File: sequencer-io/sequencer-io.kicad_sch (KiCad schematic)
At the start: 97 parts, among them SW1 SW_Push, SW10 SW_Push, SW11 SW_Push, SW12 SW_Push, SW13 SW_Push, SW14 SW_Push, SW15 SW_Push, SW16 SW_Push, SW17 SW_Push, SW18 SW_Push, SW19 SW_Push, SW2 SW_Push, SW20 SW_Push, SW21 SW_Push, SW22 SW_Push, SW23 SW_Push, SW24 RotaryEncoder, SW3 SW_Push, SW4 SW_Push, SW5 SW_Push, SW6 SW_Push, SW7 SW_Push, SW8 SW_Push, SW9 SW_Push, U2 74HC595, U20 SC0915

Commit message: Edited PCB
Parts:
- added D24: 1N4148W, Diode_SMD:D_SOD-323_HandSoldering, symbol Diode:1N4148W
- U20: footprint SC0915:MODULE_SC0915 -> SC0915:SC0915
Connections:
- net +5V: now also U20.40 (VBUS), D24.2 (A)
- net COL0: now also U20.21 (GP16); no longer U20.10 (GP7)
- net COL1: now also U20.22 (GP17); no longer U20.9 (GP6)
- net COL2: now also U20.24 (GP18); no longer U20.7 (GP5)
- net COL3: now also U20.25 (GP19); no longer U20.6 (GP4)
- net COL4: now also U20.26 (GP20); no longer U20.5 (GP3)
- net COL5: now also U20.27 (GP21); no longer U20.4 (GP2)
- net COL6: now also U20.29 (GP22); no longer U20.2 (GP1)
- net COL7: now also U20.31 (GP26); no longer U20.1 (GP0)
- net DIGIT_1: now also U20.17 (GP13)
- net DIGIT_2: now also U20.16 (GP12)
- net DIGIT_3: now also U20.15 (GP11)
- net ENC_A: now also U20.19 (GP14)
- net ENC_B: now also U20.20 (GP15)
- net GND: now also U20.13 (GND), U20.18 (GND), U20.23 (GND), U20.28 (GND), U20.3 (GND), U20.33 (AGND), U20.38 (GND), U20.8 (GND), U20.D2 (GND)
- net PXL: now also U20.34 (GP28); no longer U20.16 (GP12)
- net ROW0: now also U20.4 (GP2); no longer U20.11 (GP8)
- net ROW1: now also U20.5 (GP3); no longer U20.12 (GP9)
- net ROW2: now also U20.6 (GP4); no longer U20.14 (GP10)
- net ROW3: now also U20.7 (GP5); no longer U20.15 (GP11)
- net VSYS: now reaches U20.39 (VSYS)
- net VSYS: now also D24.1 (K)
- no-connect marks 1 -> 2

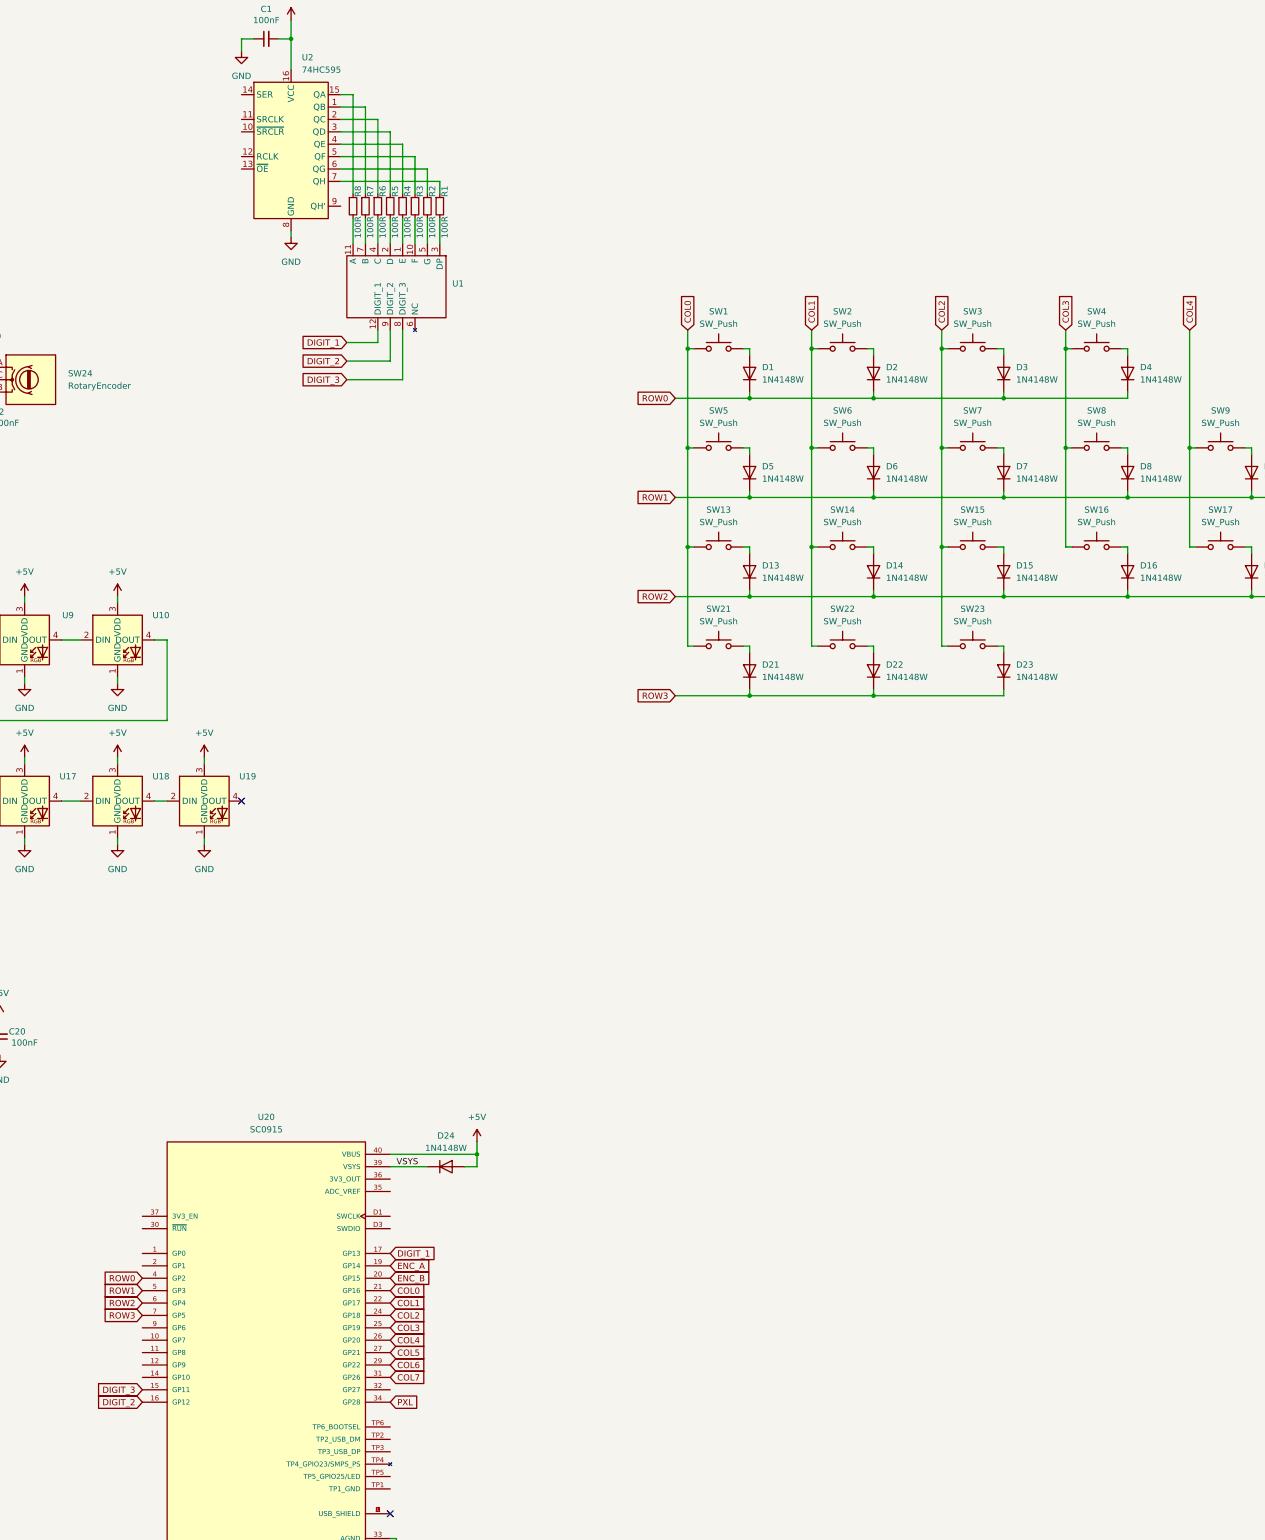
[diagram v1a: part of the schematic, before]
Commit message: Added TCA8418
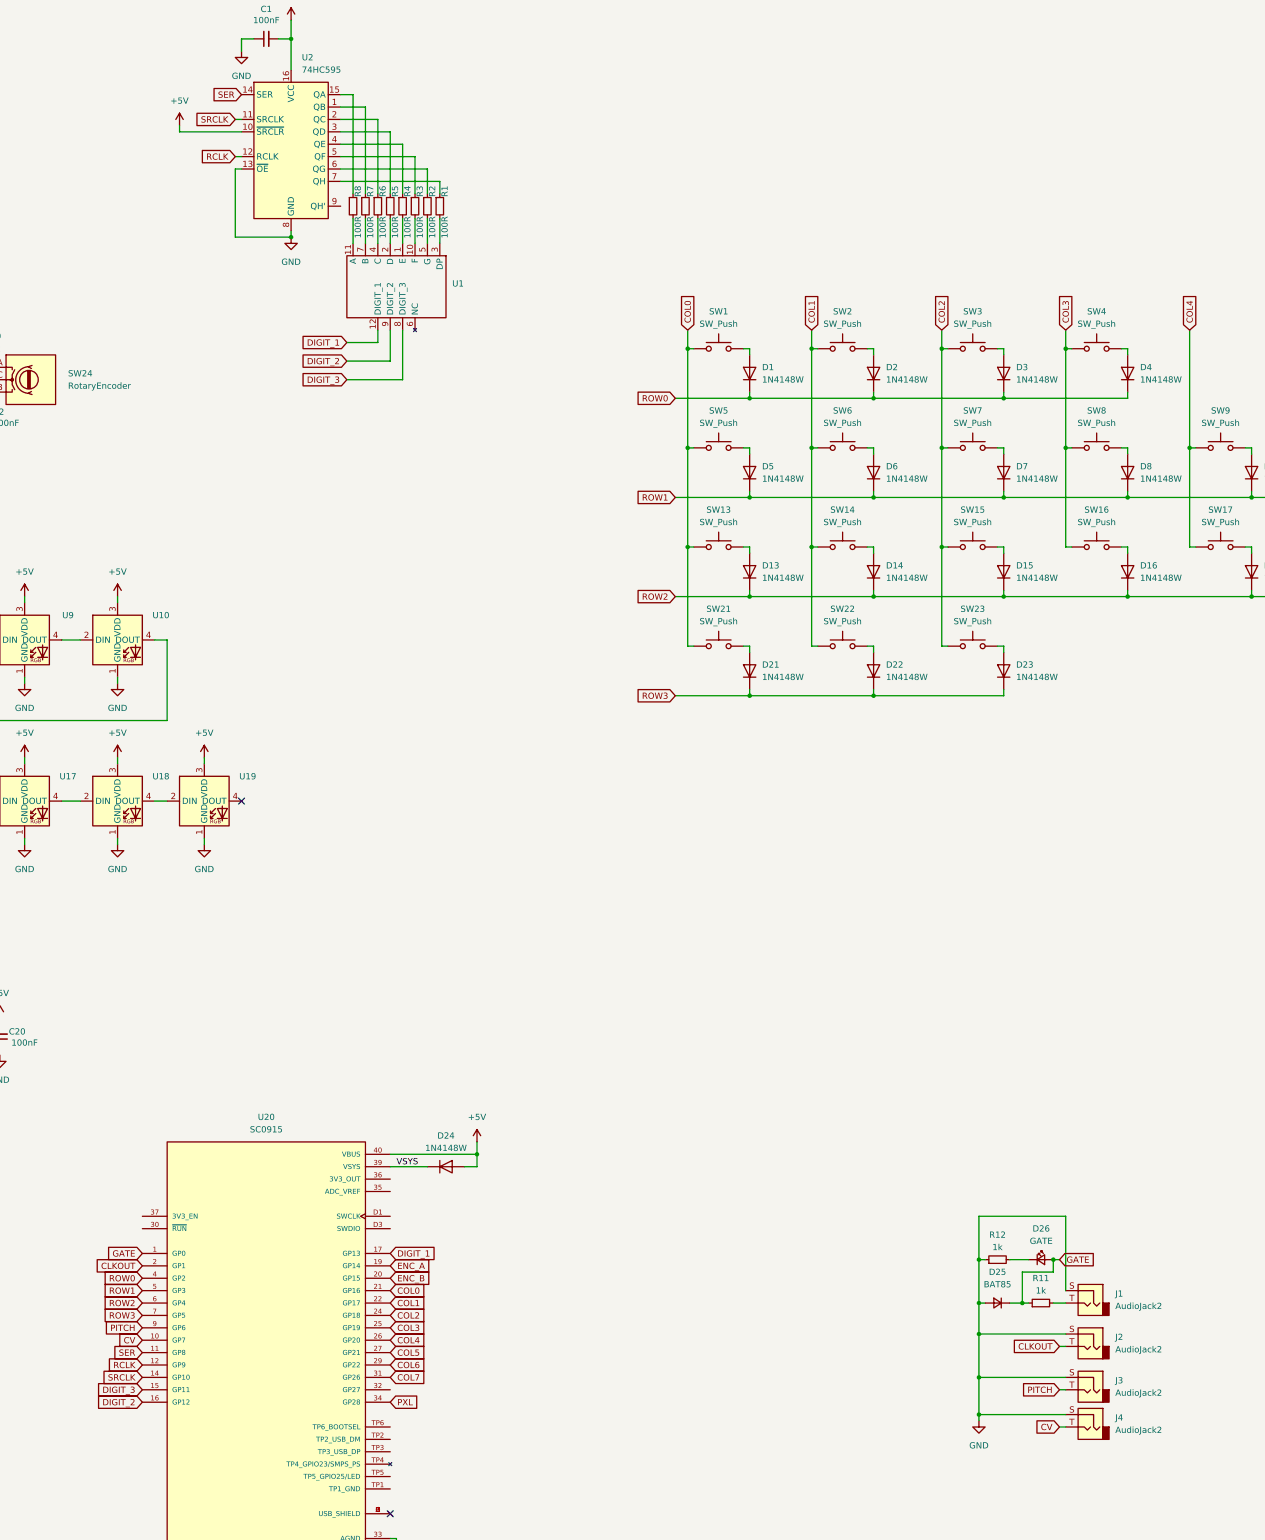
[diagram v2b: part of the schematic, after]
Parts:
- added D25: BAT85, symbol Device:D_Small
- added D26: GATE, symbol Device:LED_Small
- added J1, J2, J3, J4: AudioJack2, symbol Connector_Audio:AudioJack2
- added R11, R12: 1k, symbol Device:R_Small
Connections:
- net +5V: now also U2.10 (~{SRCLR})
- net GND: now also U2.13 (~{OE}), D25.2 (A), J1.S, J2.S, J3.S, J4.S, R12.1
- net GATE: now reaches U20.1 (GP0)
- net GATE: now also D25.1 (K), D26.2 (A), R11.1
- net CV: now reaches U20.10 (GP7)
- net CV: now also J4.T
- net SER: now reaches U20.11 (GP8)
- net SER: now also U2.14 (SER)
- net RCLK: now reaches U20.12 (GP9)
- net RCLK: now also U2.12 (RCLK)
- net SRCLK: now reaches U20.14 (GP10)
- net SRCLK: now also U2.11 (SRCLK)
- net CLKOUT: now reaches U20.2 (GP1)
- net CLKOUT: now also J2.T
- net PITCH: now reaches U20.9 (GP6)
- net PITCH: now also J3.T
- new net: J1.T, R11.2
- new net: D26.1 (K), R12.2

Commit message: Cleaned up schematic, added DAC and outputs
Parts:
- removed C1, C10, C11, C12, C13, C14, C15, C16, C17, C18, C19, C2, C20, C3, C4, C5, C6, C7, C8, C9: 100nF, Capacitor_SMD:C_0603_1608Metric_Pad1.08x0.95mm_HandSolder, symbol Device:C_Small
- removed D1, D10, D11, D12, D13, D14, D15, D16, D17, D18, D19, D2, D20, D21, D22, D23, D24, D3, D4, D5, D6, D7, D8, D9: 1N4148W, Diode_SMD:D_SOD-323_HandSoldering, symbol Diode:1N4148W
- removed D25: BAT85, symbol Device:D_Small
- removed D26: GATE, symbol Device:LED_Small
- removed J1, J2, J3, J4: AudioJack2, symbol Connector_Audio:AudioJack2
- removed R1, R2, R3, R4, R5, R6, R7, R8: 100R, Resistor_SMD:R_0603_1608Metric_Pad0.98x0.95mm_HandSolder, symbol Device:R_Small
- removed R10, R9: 1k, Resistor_SMD:R_0603_1608Metric_Pad0.98x0.95mm_HandSolder, symbol Device:R_Small
- removed R11, R12: 1k, symbol Device:R_Small
- removed SW1, SW10, SW11, SW12, SW13, SW14, SW15, SW16, SW17, SW18, SW19, SW2, SW20, SW23, SW3, SW4, SW5, SW6, SW7, SW8, SW9: SW_Push, PCM_Switch_Keyboard_Cherry_MX:SW_Cherry_MX_PCB_1.00u, symbol Switch:SW_Push
- removed SW21, SW22: SW_Push, PCM_Switch_Keyboard_Cherry_MX:SW_Cherry_MX_PCB_2.00u, symbol Switch:SW_Push
- removed SW24: RotaryEncoder, EC12E2430404:EC12E2430404, symbol Device:RotaryEncoder
- removed U1: ~, FJ5361BH:FJ5361BH, symbol FJ5361BH:FJ5361BH
- removed U10, U11, U12, U13, U14, U15, U16, U17, U18, U19, U3, U4, U5, U6, U7, U8, U9: ~, SK6812MINI-E-012:SK6812MINI-E-012, symbol SK6812MINI-E-012:SK6812MINI-E-012
- removed U2: 74HC595, Package_SO:SOIC-16_3.9x9.9mm_P1.27mm, symbol 74xx:74HC595
- added C21: 47uF, Capacitor_SMD:C_0603_1608Metric_Pad1.08x0.95mm_HandSolder, symbol Device:C_Small
- added D26: SS34F, Diode_SMD:D_SMA_Handsoldering, symbol Device:D_Schottky_Small
- added J7: 5V EXT, Connector_PinHeader_2.54mm:PinHeader_1x02_P2.54mm_Vertical, symbol Connector_Generic:Conn_01x02
- added Q7: DMG2305UX-7, Package_TO_SOT_SMD:SOT-23, symbol Device:Q_PMOS_GSD
- added R19, R20: 10k, Resistor_SMD:R_0603_1608Metric_Pad0.98x0.95mm_HandSolder, symbol Device:R_Small
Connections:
- net VSYS is gone; now on net +5V: U20.39 (VSYS)
- net +5V: now also C21.2, D26.1 (K), Q7.2 (S); no longer U20.40 (VBUS)
- net GND: now also C21.1, J7.2 (Pin_2)
- net CLKOUT: no longer names the net of U20.2 (GP1)
- net COL0: no longer names the net of U20.21 (GP16)
- net COL1: no longer names the net of U20.22 (GP17)
- net COL2: no longer names the net of U20.24 (GP18)
- net COL3: no longer names the net of U20.25 (GP19)
- net COL4: no longer names the net of U20.26 (GP20)
- net COL5: no longer names the net of U20.27 (GP21)
- net COL6: no longer names the net of U20.29 (GP22)
- net COL7: no longer names the net of U20.31 (GP26)
- net CV: no longer names the net of U20.10 (GP7)
- net DIGIT_1: no longer names the net of U20.17 (GP13)
- net DIGIT_2: no longer names the net of U20.16 (GP12)
- net DIGIT_3: no longer names the net of U20.15 (GP11)
- net ENC_A: no longer names the net of U20.19 (GP14)
- net ENC_B: no longer names the net of U20.20 (GP15)
- net GATE: no longer names the net of U20.1 (GP0)
- net PITCH: no longer names the net of U20.9 (GP6)
- net PXL: no longer names the net of U20.34 (GP28)
- net RCLK: no longer names the net of U20.12 (GP9)
- net ROW0: no longer names the net of U20.4 (GP2)
- net ROW1: no longer names the net of U20.5 (GP3)
- net ROW2: no longer names the net of U20.6 (GP4)
- net ROW3: no longer names the net of U20.7 (GP5)
- net SER: no longer names the net of U20.11 (GP8)
- net SRCLK: no longer names the net of U20.14 (GP10)
- new net: D26.2 (A), Q7.1 (G), U20.40 (VBUS)
- new net: J7.1 (Pin_1), Q7.3 (D)
- new net +3.3V: R19.1, R20.1
- new net Switches/SCL: R20.2
- new net Switches/SDA: R19.2
- no-connect marks 2 -> 7
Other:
- added sheet DAC (dac.kicad_sch)
- added sheet IOs (ios.kicad_sch)
- added sheet LEDs (leds.kicad_sch)
- added sheet Switches (switches.kicad_sch)
- moved on the sheet: U20

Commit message: lil update
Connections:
- net LEDs/PXL: now also U20.20 (GP15)
- net Switches/SCL: now also U20.2 (GP1)
- net Switches/SDA: now also U20.1 (GP0)
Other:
- moved on the sheet: C21, D26, J7, Q7, U20

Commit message: edits
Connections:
- net IOs/DIGIT_1: now also U20.26 (GP20)
- net IOs/DIGIT_2: now also U20.25 (GP19)
- net IOs/DIGIT_3: now also U20.24 (GP18)
- net IOs/ENC_A: now also U20.20 (GP15)
- net IOs/ENC_B: now also U20.19 (GP14)
- net LEDs/PXL: now also U20.34 (GP28); no longer U20.20 (GP15)
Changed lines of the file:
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@@
+	(wire
+		(pts
+			(xy 85.09 80.01) (xy 85.09 137.16)
+		)
+		(stroke
+			(width 0)
+			(type default)
+		)
+	)
 	(wire
 		(pts
@@
 	(wire
 		(pts
+			(xy 63.5 95.25) (xy 82.55 95.25)
+		)
+		(stroke
+			(width 0)
+			(type default)
+		)
+	)
+	(wire
+		(pts
 			(xy 161.29 36.83) (xy 161.29 38.1)
 		)
@@
 	(wire
 		(pts
+			(xy 87.63 134.62) (xy 151.13 134.62)
+		)
+		(stroke
+			(width 0)
+			(type default)
+		)
+	)
+	(wire
+		(pts
 			(xy 69.85 123.19) (xy 63.5 123.19)
 		)
@@
 	(wire
 		(pts
+			(xy 153.67 77.47) (xy 153.67 137.16)
+		)
+		(stroke
+			(width 0)
+			(type default)
+		)
+	)
+	(wire
+		(pts
 			(xy 67.31 142.24) (xy 67.31 85.09)
 		)
@@
 	(wire
 		(pts
+			(xy 83.82 92.71) (xy 83.82 138.43)
+		)
+		(stroke
+			(width 0)
+			(type default)
+		)
+	)
+	(wire
+		(pts
+			(xy 152.4 135.89) (xy 152.4 80.01)
+		)
+		(stroke
+			(width 0)
+			(type default)
+		)
+	)
+	(wire
+		(pts
 			(xy 175.26 34.29) (xy 181.61 34.29)
 		)
@@
 	(wire
 		(pts
+			(xy 82.55 139.7) (xy 156.21 139.7)
+		)
+		(stroke
+			(width 0)
+			(type default)
+		)
+	)
+	(wire
+		(pts
 			(xy 144.78 125.73) (xy 146.05 125.73)
 		)
@@
 	(wire
 		(pts
+			(xy 85.09 137.16) (xy 153.67 137.16)
+		)
+		(stroke
+			(width 0)
+			(type default)
+		)
+	)
+	(wire
+		(pts
+			(xy 86.36 135.89) (xy 152.4 135.89)
+		)
+		(stroke
+			(width 0)
+			(type default)
+		)
+	)
+	(wire
+		(pts
+			(xy 151.13 82.55) (xy 151.13 134.62)
+		)
+		(stroke
+			(width 0)
+			(type default)
+		)
+	)
+	(wire
+		(pts
+			(xy 63.5 74.93) (xy 87.63 74.93)
+		)
+		(stroke
+			(width 0)
+			(type default)
+		)
+	)
+	(wire
+		(pts
 			(xy 73.66 52.07) (xy 73.66 53.34)
 		)
@@
 	(wire
 		(pts
+			(xy 152.4 80.01) (xy 144.78 80.01)
+		)
+		(stroke
+			(width 0)
+			(type default)
+		)
+	)
+	(wire
+		(pts
 			(xy 64.77 64.77) (xy 93.98 64.77)
 		)
@@
 	(wire
 		(pts
+			(xy 156.21 139.7) (xy 156.21 67.31)
+		)
+		(stroke
+			(width 0)
+			(type default)
+		)
+	)
+	(wire
+		(pts
 			(xy 64.77 58.42) (xy 64.77 64.77)
 		)
@@
 	(wire
 		(pts
+			(xy 63.5 92.71) (xy 83.82 92.71)
+		)
+		(stroke
+			(width 0)
+			(type default)
+		)
+	)
+	(wire
+		(pts
+			(xy 86.36 77.47) (xy 86.36 135.89)
+		)
+		(stroke
+			(width 0)
+			(type default)
+		)
+	)
+	(wire
+		(pts
 			(xy 160.02 36.83) (xy 161.29 36.83)
 		)
@@
 	(wire
 		(pts
+			(xy 83.82 138.43) (xy 154.94 138.43)
+		)
+		(stroke
+			(width 0)
+			(type default)
+		)
+	)
+	(wire
+		(pts
 			(xy 72.39 152.4) (xy 72.39 120.65)
 		)
@@
 	(wire
 		(pts
-			(xy 144.78 69.85) (xy 168.91 69.85)
+			(xy 156.21 67.31) (xy 144.78 67.31)
+		)
+		(stroke
+			(width 0)
+			(type default)
+		)
+	)
+	(wire
+		(pts
+			(xy 63.5 77.47) (xy 86.36 77.47)
+		)
+		(stroke
+			(width 0)
+			(type default)
+		)
+	)
+	(wire
+		(pts
+			(xy 144.78 95.25) (xy 168.91 95.25)
+		)
+		(stroke
+			(width 0)
+			(type default)
+		)
+	)
+	(wire
+		(pts
+			(xy 87.63 74.93) (xy 87.63 134.62)
 		)
 		(stroke
@@
 	(wire
 		(pts
+			(xy 63.5 80.01) (xy 85.09 80.01)
+		)
+		(stroke
+			(width 0)
+			(type default)
+		)
+	)
+	(wire
+		(pts
+			(xy 82.55 95.25) (xy 82.55 139.7)
+		)
+		(stroke
+			(width 0)
+			(type default)
+		)
+	)
+	(wire
+		(pts
 			(xy 144.78 123.19) (xy 146.05 123.19)
 		)
@@
 	(wire
 		(pts
+			(xy 144.78 82.55) (xy 151.13 82.55)
+		)
+		(stroke
+			(width 0)
+			(type default)
+		)
+	)
+	(wire
+		(pts
 			(xy 73.66 58.42) (xy 73.66 67.31)
 		)
@@
 	(wire
 		(pts
+			(xy 144.78 77.47) (xy 153.67 77.47)
+		)
+		(stroke
+			(width 0)
+			(type default)
+		)
+	)
+	(wire
+		(pts
+			(xy 154.94 69.85) (xy 144.78 69.85)
+		)
+		(stroke
+			(width 0)
+			(type default)
+		)
+	)
+	(wire
+		(pts
 			(xy 181.61 33.02) (xy 181.61 34.29)
 		)
@@
 		(pts
 			(xy 181.61 44.45) (xy 179.07 44.45)
+		)
+		(stroke
+			(width 0)
+			(type default)
+		)
+	)
+	(wire
+		(pts
+			(xy 154.94 138.43) (xy 154.94 69.85)
 		)
 		(stroke
@@
 	)
 	(sheet
-		(at 168.91 67.31)
+		(at 168.91 92.71)
 		(size 12.7 5.08)
 		(fields_autoplaced yes)
@@
 		)
 		(property "Sheetname" "LEDs"
-			(at 168.91 66.5984 0)
+			(at 168.91 91.9984 0)
 			(effects
 				(font
@@
 		)
 		(property "Sheetfile" "leds.kicad_sch"
-			(at 168.91 72.9746 0)
+			(at 168.91 98.3746 0)
 			(effects
 				(font
@@
 		)
 		(pin "PXL" input
-			(at 168.91 69.85 180)
-			(effects
-				(font
+			(at 168.91 95.25 180)
+			(effects
+				(font
